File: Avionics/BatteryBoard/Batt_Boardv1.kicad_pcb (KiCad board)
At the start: 2 copper layers, 90.2 x 95.9 mm, 30 parts, among them J1 Conn_02x26_Odd_Even, J2 Conn_02x26_Odd_Even, Q1 IRF7458, Q2 IRF7458

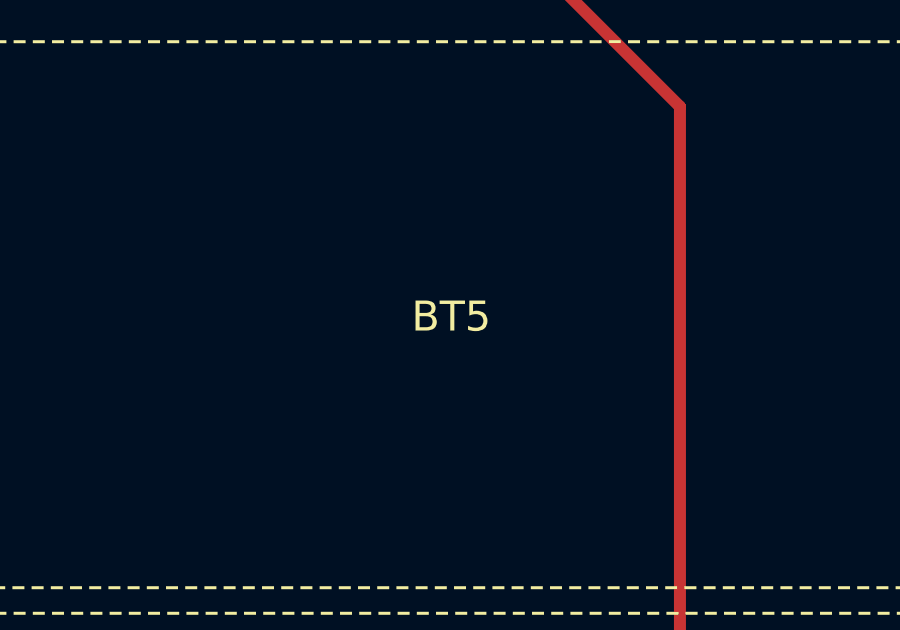
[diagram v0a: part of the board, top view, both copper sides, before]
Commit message: batt_brd: Update battery footprints
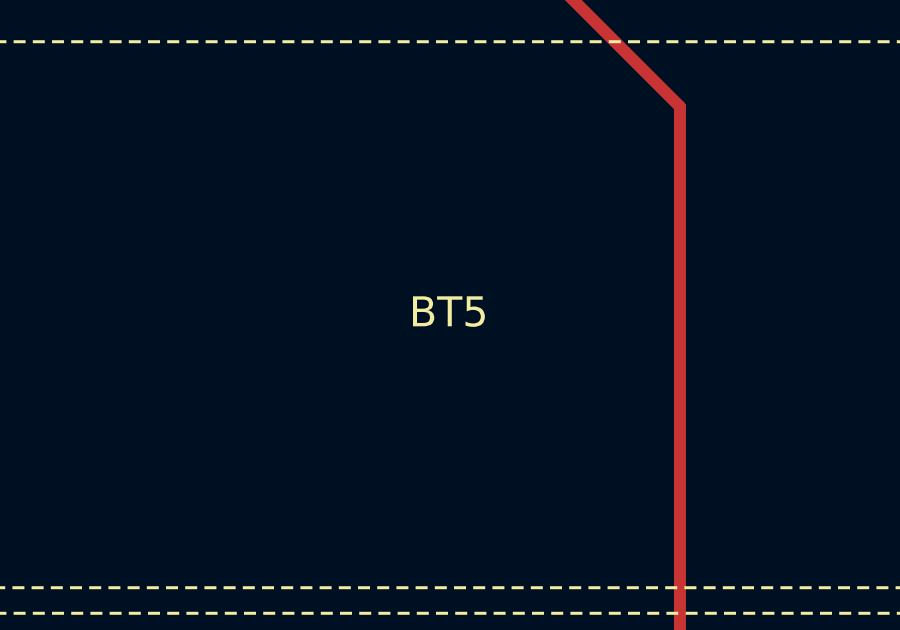
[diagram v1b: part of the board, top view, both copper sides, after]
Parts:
- BT1, BT16, BT2, BT3, BT4, BT5: footprint 254:BAT_254_1 -> BattBrdFtPrts:BAT_254_1

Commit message: "Finish" routing
DRC failing; will fix soon
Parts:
- removed BT1, BT16, BT2, BT3, BT4, BT5: 54, BattBrdFtPrts:BAT_254_1
- removed R5460: ~, Package_TO_SOT_SMD:SOT-23-6
- added BT_H_1: 54, BattBrdFtPrts:BAT_254_1, B.Cu at (145.0, 131.5)
- added BT_H_2: 54, BattBrdFtPrts:BAT_254_1, B.Cu at (145.0, 112.5)
- added BT_H_3: 54, BattBrdFtPrts:BAT_254_1, B.Cu at (145.0, 93.5)
- added BT_L_1: 54, BattBrdFtPrts:BAT_254_1, F.Cu at (145.0, 74.5)
- added BT_L_2: 54, BattBrdFtPrts:BAT_254_1, F.Cu at (145.0, 93.5)
- added BT_L_3: 54, BattBrdFtPrts:BAT_254_1, B.Cu at (145.0, 74.5)
- added C10: 1uF, Capacitor_SMD:C_0805_2012Metric, F.Cu at (128.0, 118.0)
- added C11: 2.2uF, Capacitor_SMD:C_0805_2012Metric, F.Cu at (128.0, 124.5)
- added C12: 15pF, Capacitor_SMD:C_0805_2012Metric, F.Cu at (118.0, 111.0)
- added C13: 0.1uF, Capacitor_SMD:C_0805_2012Metric, F.Cu at (123.0, 120.5)
- added C14: 0.1uF, Capacitor_SMD:C_0805_2012Metric, F.Cu at (120.0, 106.9)
- added C2: 0.1uF, Capacitor_SMD:C_0805_2012Metric, F.Cu at (181.0, 113.5)
- added C7: 0.33uF, Capacitor_SMD:C_0805_2012Metric, F.Cu at (139.0, 114.0)
- added C8: 0.1uF, Capacitor_SMD:C_0805_2012Metric, F.Cu at (154.5, 109.5)
- added C9: 0.1uF, Capacitor_SMD:C_0805_2012Metric, F.Cu at (147.8, 112.5)
- added R12: 100, Resistor_SMD:R_0805_2012Metric, F.Cu at (147.8, 108.0)
- added R13: 10k, Resistor_SMD:R_0805_2012Metric, F.Cu at (107.0, 120.2)
- added R14: 31.6k, Resistor_SMD:R_0805_2012Metric, F.Cu at (111.1, 121.5)
- added R15: 1.5k, Resistor_SMD:R_0805_2012Metric, F.Cu at (107.0, 122.7)
- added R2: 1K, Resistor_SMD:R_0603_1608Metric, F.Cu at (175.5, 124.0)
- added R7: 160, Resistor_SMD:R_0805_2012Metric, F.Cu at (143.5, 105.6)
- added R8: 260, Resistor_SMD:R_0805_2012Metric, F.Cu at (134.0, 110.0)
- added R9: 100, Resistor_SMD:R_0805_2012Metric, F.Cu at (134.0, 114.0)
- added U10: LMV331, Package_TO_SOT_SMD:SOT-23-5, F.Cu at (118.0, 115.0)
- added U11: TPS7A2601DRVR, BattBrdFtPrts:DRV0006A_NV, F.Cu at (128.0, 122.0)
- added U13: 74AHC1G32, Package_TO_SOT_SMD:SOT-23-5, F.Cu at (123.5, 107.0)
- added U14: 74AHC1G04, Package_TO_SOT_SMD:SOT-23-5, F.Cu at (123.2, 117.4)
- added U15: 74LVC2G08, Package_SO:VSSOP-8_2.3x2mm_P0.5mm, F.Cu at (123.5, 111.0)
- added U2: BQ29200DRBR, BattBrdFtPrts:DRB8_1P6X2P4, F.Cu at (143.4, 110.3)
- added U3: TLA2024IRUGR, BattBrdFtPrts:RUG10_TEX, F.Cu at (154.5, 112.8)
- added U4: LM35-LP, Package_TO_SOT_THT:TO-92_Inline, F.Cu at (135.3, 121.9)
- added U5: LM35-LP, Package_TO_SOT_THT:TO-92_Inline, F.Cu at (142.3, 121.9)
- added U6: LM35-LP, Package_TO_SOT_THT:TO-92_Inline, F.Cu at (156.2, 121.9)
- added U7: LM35-LP, Package_TO_SOT_THT:TO-92_Inline, F.Cu at (149.3, 121.9)
- added U8: LM4040DBZ-2.5, Package_TO_SOT_SMD:SOT-23, F.Cu at (110.2, 126.2)
- added U9: TMP36xS, Package_TO_SOT_THT:TO-92_Inline, F.Cu at (114.5, 122.0)
- C1, C3, C4, C5, C6: footprint Capacitor_SMD:C_0603_1608Metric -> Capacitor_SMD:C_0805_2012Metric
- R3: value 1K -> 330
- R5: value 330 -> >47k; footprint Resistor_SMD:R_0603_1608Metric -> Resistor_SMD:R_0805_2012Metric
- U1: value ~ -> R5460N210AD1; footprint Package_SO:SOIC-8_3.9x4.9mm_P1.27mm -> Package_TO_SOT_SMD:SOT-23-6
- moved C4 54.7 mm to (178.5, 113.5), turned to -90 degrees
- moved R4 54.4 mm to (180.5, 118.0), turned to 90 degrees
- moved TP2 53.2 mm to (116.5, 143.5), turned to 90 degrees
- moved TP4 52.4 mm to (112.5, 143.5), turned to 90 degrees
- moved R3 50.0 mm to (178.5, 118.0)
- moved TP1 49.8 mm to (124.5, 143.5), turned to 90 degrees
- moved TP3 47.1 mm to (120.5, 143.5), turned to 90 degrees
- moved C3 46.0 mm to (174.5, 114.5), turned to 180 degrees
- moved R1 44.1 mm to (172.5, 110.0), turned to 180 degrees
- moved C1 39.0 mm to (169.5, 114.0), turned to -90 degrees
- moved Q1 29.5 mm to (164.5, 109.5), turned to 180 degrees
- moved Q2 27.9 mm to (164.5, 115.4), turned to 180 degrees
- moved U1 23.5 mm to (173.5, 119.0), turned to 90 degrees
- moved C5 18.5 mm to (138.3, 106.5), turned to -90 degrees
- moved C6 16.9 mm to (138.3, 110.5), turned to -90 degrees
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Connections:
- C3 pad 2: Net-(R5460N210AD1-V-) -> Net-(U1-VC)
- C4 pad 2: Net-(R5460N210AD1-VC) -> /VDD
- C5 pad 1: /B- -> Net-(U2-VC2)
- C5 pad 2: /VDD -> Net-(U2-VC1)
- C6 pad 1: GNDREF -> Net-(U2-VC1)
- C6 pad 2: /3V3_BUS -> /B-
- J1 pad 37: unconnected-(J1-Pin_37-Pad37) -> KAPTON_EN
- J1 pad 38: unconnected-(J1-Pin_38-Pad38) -> KAPTON_OBC_EN
- J1 pad 41: unconnected-(J1-Pin_41-Pad41) -> /I2C1_SDA
- J1 pad 43: unconnected-(J1-Pin_43-Pad43) -> /I2C1_SCL
- J1 pad 5: /BATT_PRE_INH -> BATT_PRE_INH
- J1 pad 6: /BATT_PRE_INH -> BATT_PRE_INH
- J1 pad 7: /BATT_PRE_INH -> BATT_PRE_INH
- J1 pad 8: /BATT_PRE_INH -> BATT_PRE_INH
- J2 pad 1: /BATT_TEMP -> KAPTON_SEL
- J2 pad 25: unconnected-(J2-Pin_25-Pad25) -> +5V
- J2 pad 26: unconnected-(J2-Pin_26-Pad26) -> +5V
- J2 pad 27: /3V3_BUS -> +3V3
- J2 pad 28: /3V3_BUS -> +3V3
- R3 pad 1: Net-(R5460N210AD1-V-) -> /BM
- R3 pad 2: GNDREF -> Net-(U1-VC)
- R4 pad 1: /BM -> BATT_PRE_INH
- R4 pad 2: Net-(R5460N210AD1-VC) -> /VDD
- R5 pad 1: /BATT_PRE_INH -> +5VA
- R5 pad 2: /VDD -> /Heater Control/COMP_OUT
- TP4 pad 1: /BATT_PRE_INH -> BATT_PRE_INH
- U1 pad 1: /BATT_TEMP -> Net-(Q1-G)
- U1 pad 2: unconnected-(U1-NC_2-Pad2) -> Net-(Q2-G)
- U1 pad 3: unconnected-(U1-NC_3-Pad3) -> Net-(U1-V-)
- U1 pad 4: GNDREF -> Net-(U1-VC)
- U1 pad 5: /3V3_BUS -> /VDD
- U1 pad 6: unconnected-(U1-NC_4-Pad6) -> /B-
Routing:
- net /B-: track 76.0 -> 203.1 mm, vias 9 -> 12
- net +5V: track 0.00 -> 111.1 mm, vias 0 -> 2
- net KAPTON_SEL: track 0.00 -> 79.3 mm, vias 0 -> 2
- net +5VA: track 0.00 -> 78.0 mm, vias 0 -> 4
- net /BATT_TEMP: track 75.1 -> 0.00 mm
- net /3V3_BUS: track 72.5 -> 0.00 mm
- net KAPTON_OBC_EN: track 0.00 -> 69.6 mm, vias 0 -> 3
- net KAPTON_EN: track 0.00 -> 59.8 mm, vias 0 -> 3
- net /I2C1_SCL: track 0.00 -> 55.9 mm, vias 0 -> 3
- net /I2C1_SDA: track 0.00 -> 54.0 mm, vias 0 -> 4
- net /BATT_PRE_INH: track 52.7 -> 0.00 mm
- net /BM: track 44.5 -> 95.2 mm, vias 21 -> 44
- net Net-(U3-AIN0): track 0.00 -> 22.8 mm
- net Net-(U1-V-): track 0.00 -> 16.8 mm
- net Net-(U3-AIN1): track 0.00 -> 16.4 mm
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- added copper zone on B.Cu, net BATT_PRE_INH
- added copper zone on B.Cu, net GNDREF
- added copper zone on F.Cu, net Net-(C1-Pad1)
- added copper zone on F.Cu, net Net-(Q1-D-Pad5)
- removed copper zone on B.Cu, net /BATT_PRE_INH

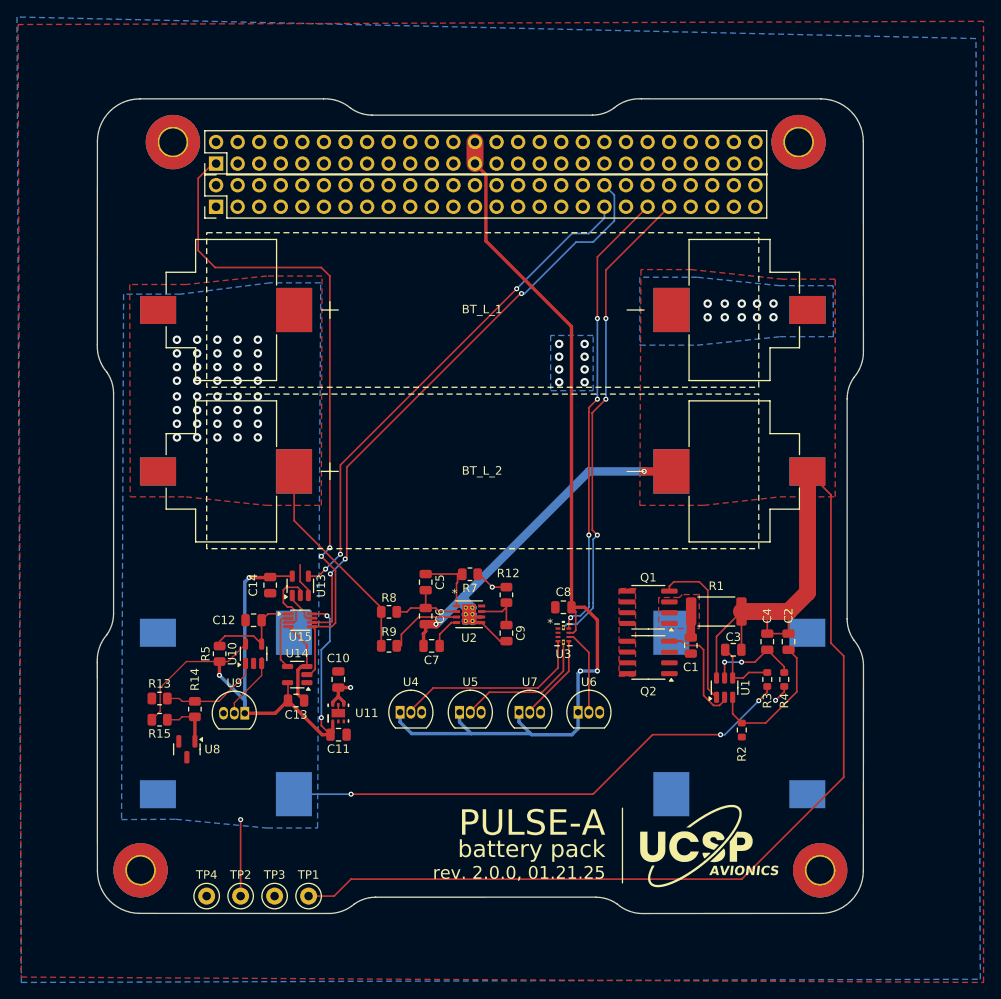
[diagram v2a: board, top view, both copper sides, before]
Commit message: resolve some drc things; add custom jlc drc rules
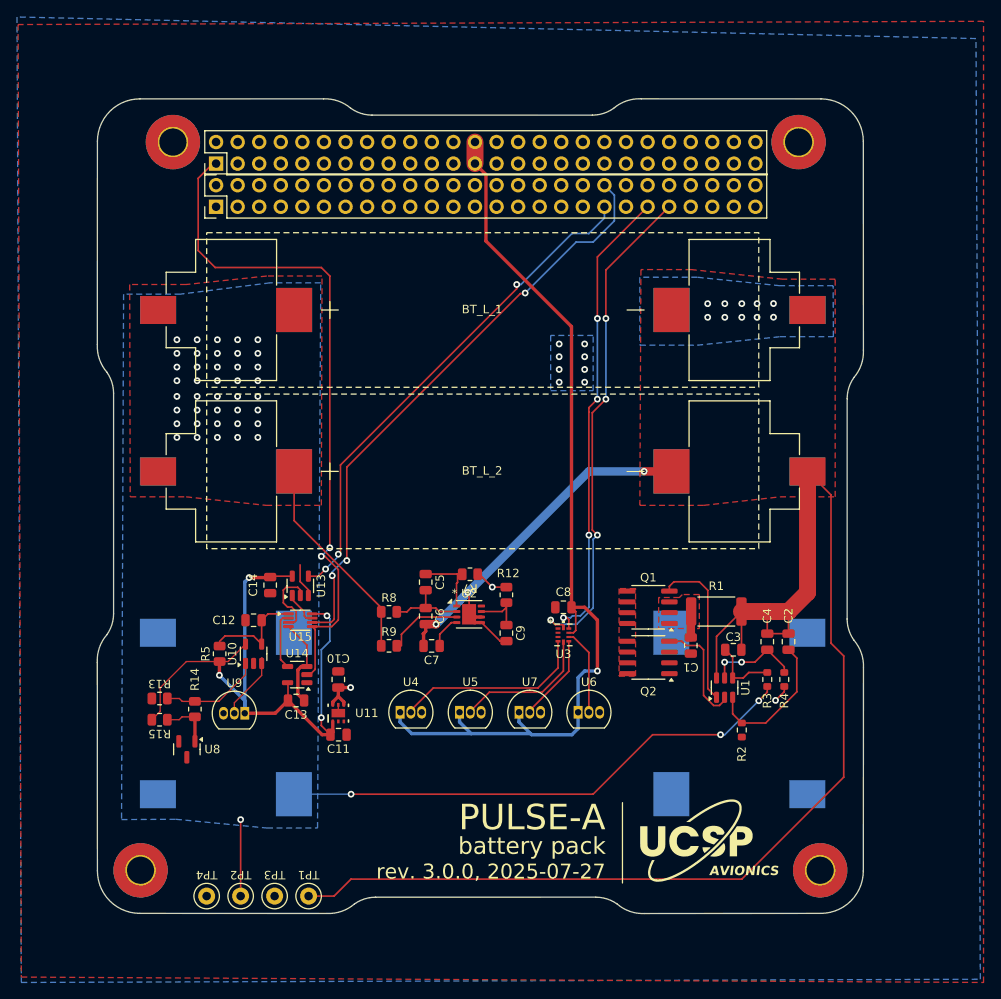
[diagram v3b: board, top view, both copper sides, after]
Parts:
- U2: footprint BattBrdFtPrts:DRB8_1P6X2P4 -> Package_SON:VSON-8-1EP_3x3mm_P0.65mm_EP1.65x2.4mm
- moved G*** 0.64 mm to (170.0, 137.0)
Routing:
- net /B-: track 203.1 -> 198.8 mm, vias 12 -> 13
- net /I2C1_SCL: track 55.9 -> 59.5 mm, vias 3 -> 4
- net /I2C1_SDA: track 54.0 -> 55.3 mm
- net KAPTON_SEL: track 79.3 -> 79.9 mm
- net +5V: track 111.1 -> 110.8 mm, vias 2 -> 1
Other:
- board text added: "rev. 3.0.0, 2025-07-27"
- board text removed: "rev. 2.0.0, 01.21.25"
